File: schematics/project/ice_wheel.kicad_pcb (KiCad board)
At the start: 2 copper layers, 16 parts, among them Q1 BSS123, U1 OPA320xxDBV, U1 Teensy4.1, U2 PropShieldMotionSens, U3 OPA320xxDBV

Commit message: some progress, dust slowly clears
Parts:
- added D1: PMEG40T20ER, Diode_SMD:Nexperia_CFP3_SOD-123W, F.Cu at (61.0, 94.0)
- added D2: PMEG40T20ER, Diode_SMD:Nexperia_CFP3_SOD-123W, F.Cu at (61.0, 97.2)
- added J1: Conn_01x02, Connector_JST:JST_SHL_SM02B-SHLS-TF_1x02-1MP_P1.00mm_Horizontal, F.Cu at (34.8, 112.1)
- added Q1: BSS123, Package_TO_SOT_SMD:SOT-23, F.Cu at (43.6, 94.6)
- added Q2: BSS123, Package_TO_SOT_SMD:SOT-23, F.Cu at (33.8, 94.6)
- added Q3: BSS123, Package_TO_SOT_SMD:SOT-23, F.Cu at (38.7, 99.0)
- added Q4: BSS123, Package_TO_SOT_SMD:SOT-23, F.Cu at (38.7, 94.6)
- added Q5: BSS123, Package_TO_SOT_SMD:SOT-23, F.Cu at (33.8, 99.0)
- added Q6: BSS123, Package_TO_SOT_SMD:SOT-23, F.Cu at (33.8, 103.5)
- added R10: 1k, Resistor_SMD:R_0603_1608Metric, F.Cu at (48.0, 93.6)
- added R11: 1k, Resistor_SMD:R_0603_1608Metric, F.Cu at (52.0, 93.6)
- added R12: 1k, Resistor_SMD:R_0603_1608Metric, F.Cu at (52.0, 96.1)
- added R13: R, Resistor_SMD:R_0603_1608Metric, F.Cu at (47.7, 110.0)
- added R4: R, Resistor_SMD:R_0603_1608Metric, F.Cu at (42.3, 102.5)
- added R5: R, Resistor_SMD:R_0603_1608Metric, F.Cu at (46.3, 101.1)
- added R6: R, Resistor_SMD:R_0603_1608Metric, F.Cu at (48.0, 96.1)
- added R7: 1k, Resistor_SMD:R_0603_1608Metric, F.Cu at (47.2, 98.6)
- added R8: 1k, Resistor_SMD:R_0603_1608Metric, F.Cu at (38.3, 102.5)
- added R9: 1k, Resistor_SMD:R_0603_1608Metric, F.Cu at (43.1, 98.1)
- moved U1 53.6 mm to (137.2, 116.8)
- moved U2 19.0 mm to (105.4, 154.9)
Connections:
- net /Motor Controller/Dig2Analog/SetSpeed_Analog renamed /Motor Controller/throttle_IN
- U1 pad 1: unconnected-(U1-Pad1) -> GND
- U1 pad 12: /Teensy/CS -> /Prop Shield/CS
- U1 pad 13: /Teensy/MOSI -> /Prop Shield/MOSI
- U1 pad 14: /Teensy/MISO -> /Prop Shield/MISO
- U1 pad 35: /Teensy/SCK -> /Prop Shield/SCK
- U1 pad 36: unconnected-(U1-Pad36) -> /Misc/footpad_a 
- U1 pad 4: /Teensy/IRQ -> /Prop Shield/IRQ
- U1 pad 40: /Teensy/SDA -> /Prop Shield/SDA
- U1 pad 41: /Teensy/SCL -> /Prop Shield/SCL
- U1 pad 46: unconnected-(U1-Pad46) -> +3V3
- U1 pad 48: unconnected-(U1-Pad48) -> +5P
- U1 pad 49: unconnected-(U1-Pad49) -> +5F
- U1 pad 64: unconnected-(U1-Pad64) -> GND

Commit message: small progress, angsthasen
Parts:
- removed the C1 at (58.4, 137.2)
- removed the C1 at (124.5, 88.9)
- removed the C2 at (57.3, 141.6)
- removed the C2 at (128.5, 91.4)
- removed the R1 at (128.5, 88.9)
- removed the R1 at (62.4, 137.2)
- removed the R2 at (53.3, 141.6)
- removed the R2 at (124.5, 93.9)
- removed the R3 at (53.3, 144.1)
- removed the R3 at (124.5, 91.4)
- removed the U1 at (109.2, 86.4)
- added C1: C, Capacitor_SMD:C_0603_1608Metric, F.Cu at (72.0, 130.1)
- added C2: 100nF 10V, Capacitor_SMD:C_0603_1608Metric, F.Cu at (77.9, 130.0)
- added R1: R, Resistor_SMD:R_0603_1608Metric, F.Cu at (70.4, 130.1)
- added R2: R, Resistor_SMD:R_0603_1608Metric, F.Cu at (75.0, 132.6)
- added R3: R, Resistor_SMD:R_0603_1608Metric, F.Cu at (74.9, 127.5)
- added RV1: TC33X-1-203E, Potentiometer_SMD:Potentiometer_Bourns_TC33X_Vertical, F.Cu at (91.3, 83.2)
- added RV2: TC33X-1-203E, Potentiometer_SMD:Potentiometer_Bourns_TC33X_Vertical, F.Cu at (91.3, 88.0)
- added RV3: TC33X-1-203E, Potentiometer_SMD:Potentiometer_Bourns_TC33X_Vertical, F.Cu at (97.5, 83.2)
- R4, R5, R6: value R -> 1k
- moved J1 154.1 mm to (188.1, 128.6)
- moved Q3 154.1 mm to (192.0, 115.5)
- moved Q4 154.1 mm to (192.0, 111.1)
- moved R10 154.1 mm to (201.3, 110.1)
- moved R6 154.1 mm to (201.3, 112.6)
- moved R8 154.1 mm to (191.5, 119.0)
- moved Q1 154.1 mm to (196.8, 111.1)
- moved Q2 154.1 mm to (187.1, 111.1)
- moved Q5 154.1 mm to (187.1, 115.5)
- moved Q6 154.1 mm to (187.1, 120.0)
- moved R11 154.1 mm to (205.3, 110.1)
- moved R12 154.1 mm to (205.3, 112.6)
- moved R13 154.1 mm to (201.0, 126.5)
- moved R4 154.1 mm to (195.5, 119.0)
- moved R5 154.1 mm to (199.5, 117.6)
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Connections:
- U1 pad 15: unconnected-(U1-Pad15) -> +3V3
- U1 pad 34: unconnected-(U1-Pad34) -> GND
- U1 pad 47: unconnected-(U1-Pad47) -> GND
- U1 pad 52: unconnected-(U1-Pad52) -> GND
- U1 pad 58: unconnected-(U1-Pad58) -> GND
- U1 pad 59: unconnected-(U1-Pad59) -> GND
- U2 pad 27: unconnected-(U2-Pad27) -> /Misc/AGND
- U2 pad 33: unconnected-(U2-Pad33) -> /Misc/AudioIN
- U2 pad 39: unconnected-(U2-Pad39) -> /Misc/Speaker+
- U2 pad 40: unconnected-(U2-Pad40) -> /Misc/Speaker-
- U2 pad 41: unconnected-(U2-Pad41) -> /Misc/5V_Speaker
- U2 pad 7: unconnected-(U2-Pad7) -> /Misc/AMP_EN
- U3 pad 1: /Motor Controller/throttle_IN -> /Motor Controller/throttle_a
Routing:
- net Net-(R2-Pad2): track 0.00 -> 6.34 mm
- net GND: track 0.00 -> 6.10 mm
- net Net-(C1-Pad1): track 0.00 -> 3.47 mm
- net +5V: track 0.00 -> 1.83 mm
- net /Motor Controller/throttle_a: track 0.00 -> 1.64 mm

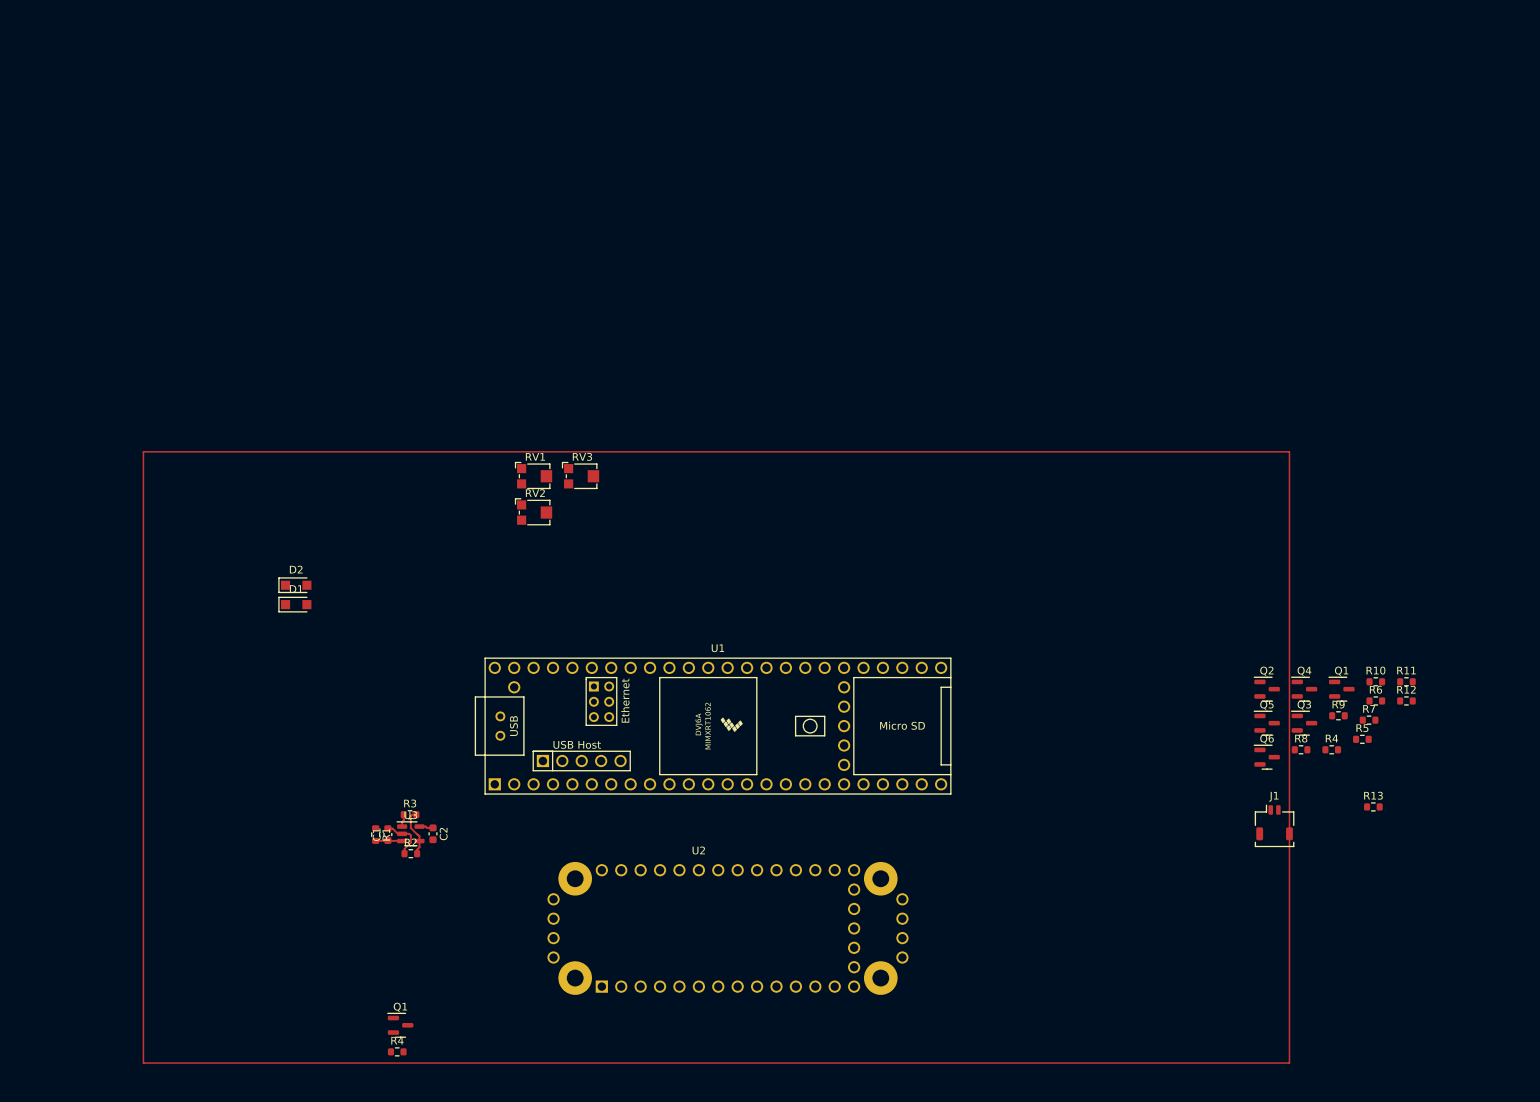
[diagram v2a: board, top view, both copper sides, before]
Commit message: Adding separate library, BT Module
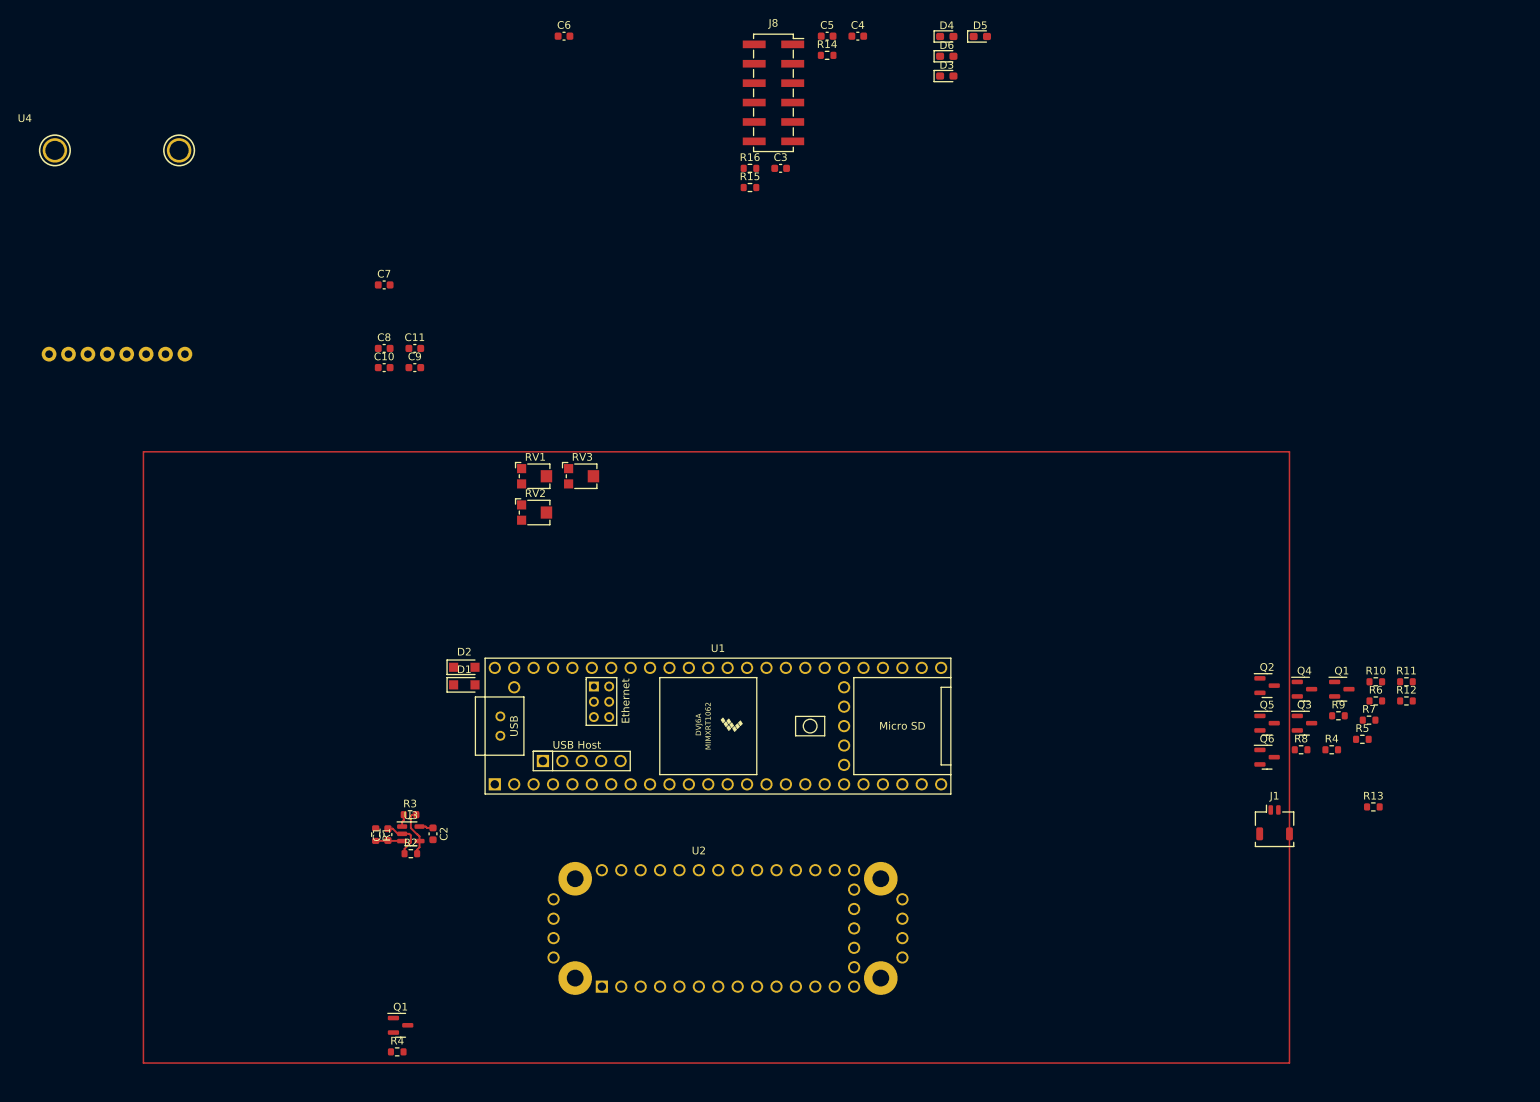
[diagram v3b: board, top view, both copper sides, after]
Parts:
- added C10: 100nF 10V, Capacitor_SMD:C_0603_1608Metric, F.Cu at (71.5, 69.0)
- added C11: 1uF 10V, Capacitor_SMD:C_0603_1608Metric, F.Cu at (75.5, 66.5)
- added C3: 10nF 10V, Capacitor_SMD:C_0603_1608Metric, F.Cu at (123.4, 42.9)
- added C4: 10nF 10V, Capacitor_SMD:C_0603_1608Metric, F.Cu at (133.5, 25.6)
- added C5: 10nF 10V, Capacitor_SMD:C_0603_1608Metric, F.Cu at (129.5, 25.6)
- added C6: 1uF 10V, Capacitor_SMD:C_0603_1608Metric, F.Cu at (95.0, 25.6)
- added C7: 100nF 10V, Capacitor_SMD:C_0603_1608Metric, F.Cu at (71.5, 58.2)
- added C8: 100nF 10V, Capacitor_SMD:C_0603_1608Metric, F.Cu at (71.5, 66.5)
- added C9: 1uF 10V, Capacitor_SMD:C_0603_1608Metric, F.Cu at (75.5, 69.0)
- added D3: D3V3S1U2LP1610-7, Diode_SMD:D_0603_1608Metric_Pad1.05x0.95mm_HandSolder, F.Cu at (145.1, 30.8)
- added D4: D3V3S1U2LP1610-7, Diode_SMD:D_0603_1608Metric_Pad1.05x0.95mm_HandSolder, F.Cu at (145.1, 25.6)
- added D5: D3V3S1U2LP1610-7, Diode_SMD:D_0603_1608Metric_Pad1.05x0.95mm_HandSolder, F.Cu at (149.5, 25.6)
- added D6: D3V3S1U2LP1610-7, Diode_SMD:D_0603_1608Metric_Pad1.05x0.95mm_HandSolder, F.Cu at (145.1, 28.2)
- added J8: Conn_02x06_Odd_Even, Connector_PinSocket_2.54mm:PinSocket_2x06_P2.54mm_Vertical_SMD, F.Cu at (122.5, 33.0)
- added R14: 6.2k, Resistor_SMD:R_0603_1608Metric, F.Cu at (129.5, 28.1)
- added R15: 6.2k, Resistor_SMD:R_0603_1608Metric, F.Cu at (119.4, 45.4)
- added R16: 6.2k, Resistor_SMD:R_0603_1608Metric, F.Cu at (119.4, 42.9)
- added U4: Adafruit_Bluefruit_LE_UART_Friend, IceWheelLib:Adafruit_Bluefruit_LE_UART_Friend, F.Cu at (24.5, 36.9)
- R4, R5, R6: value 1k -> 10k
- moved D2 24.5 mm to (82.0, 108.2)
- moved D1 24.4 mm to (82.0, 110.5)
- moved Q2 0.47 mm to (187.1, 110.6)
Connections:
- net /Teensy/{poti_IN} renamed /Motor Controller/Dig2Analog/SetSpeed_PWM
- RV1 pad 1: +5V -> +3V3
- RV2 pad 1: +5V -> +3V3
- RV3 pad 1: +5V -> +3V3

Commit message: random commit
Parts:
- removed the Q1 at (73.7, 155.1)
- removed the R4 at (73.2, 158.5)
- added D7: D3V3S1U2LP1610-7, Diode_SMD:D_0603_1608Metric_Pad1.05x0.95mm_HandSolder, F.Cu at (84.0, 155.0)
- added D8: D3V3S1U2LP1610-7, Diode_SMD:D_0603_1608Metric_Pad1.05x0.95mm_HandSolder, F.Cu at (84.0, 151.0)
- added J10: Conn_01x05, Connector_JST:JST_SH_SM05B-SRSS-TB_1x05-1MP_P1.00mm_Horizontal, F.Cu at (105.0, 64.0)
- added J2: Conn_01x02, Connector_Phoenix_MSTB:PhoenixContact_MSTBA_2,5_2-G-5,08_1x02_P5.08mm_Horizontal, F.Cu at (212.0, 57.0)
- added J3: Conn_01x06, Connector_JST:JST_SH_SM06B-SRSS-TB_1x06-1MP_P1.00mm_Horizontal, F.Cu at (79.0, 155.0)
- added J4: Conn_01x02, Connector_JST:JST_SHL_SM02B-SHLS-TF_1x02-1MP_P1.00mm_Horizontal, F.Cu at (171.0, 154.0)
- added J5: Conn_01x03, Connector_JST:JST_SH_SM03B-SRSS-TB_1x03-1MP_P1.00mm_Horizontal, F.Cu at (180.0, 110.0)
- added J6: Conn_01x03, Connector_JST:JST_SH_SM03B-SRSS-TB_1x03-1MP_P1.00mm_Horizontal, F.Cu at (180.0, 102.0)
- added J7: Conn_01x03, Connector_JST:JST_SH_SM03B-SRSS-TB_1x03-1MP_P1.00mm_Horizontal, F.Cu at (180.0, 93.0)
- added J9: Conn_01x03, Connector_JST:JST_SH_SM03B-SRSS-TB_1x03-1MP_P1.00mm_Horizontal, F.Cu at (163.0, 71.0)
- J1: footprint Connector_JST:JST_SHL_SM02B-SHLS-TF_1x02-1MP_P1.00mm_Horizontal -> Connector_Phoenix_MSTB:PhoenixContact_MSTBA_2,5_2-G-5,08_1x02_P5.08mm_Horizontal
- moved D3 123.9 mm to (166.0, 153.0)
- moved J8 116.4 mm to (182.0, 133.0), turned to 180 degrees
- moved R4 105.1 mm to (101.0, 73.0), turned to 180 degrees
- moved R5 104.5 mm to (105.0, 73.0)
- moved R6 99.7 mm to (109.0, 75.0), turned to 180 degrees
- moved C6 98.0 mm to (54.0, 114.6)
- moved J1 91.1 mm to (108.5, 84.2)
- moved D4 88.5 mm to (175.0, 109.0), turned to -90 degrees
- moved D5 79.5 mm to (175.0, 101.0), turned to -90 degrees
- moved RV1 79.0 mm to (166.0, 109.0), turned to 90 degrees
- moved RV2 76.5 mm to (167.0, 99.0), turned to 90 degrees
- moved D6 70.4 mm to (175.0, 92.0), turned to -90 degrees
- moved RV3 68.6 mm to (166.0, 86.0), turned to -90 degrees
- moved C7 61.0 mm to (54.0, 116.6)
- moved C4 57.0 mm to (105.0, 75.0), turned to 180 degrees
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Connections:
- J8 pad 5: /Motor Controller/reverse_IN -> /Motor Controller/speed_slow_IN
- Q3 pad 3: /Motor Controller/reverse_IN -> /Motor Controller/speed_slow_IN
- R14 pad 2: unconnected-(R14-Pad2) -> Net-(R14-Pad2)
- R15 pad 2: unconnected-(R15-Pad2) -> Net-(R15-Pad2)
- R16 pad 2: unconnected-(R16-Pad2) -> Net-(R16-Pad2)
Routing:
- net Net-(Q1-Pad1): track 0.00 -> 2.18 mm
